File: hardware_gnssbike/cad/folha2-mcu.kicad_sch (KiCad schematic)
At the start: 7 parts, among them J201 Tag-Connect TC2030-NL, U201 MinewSemi ME54BS13

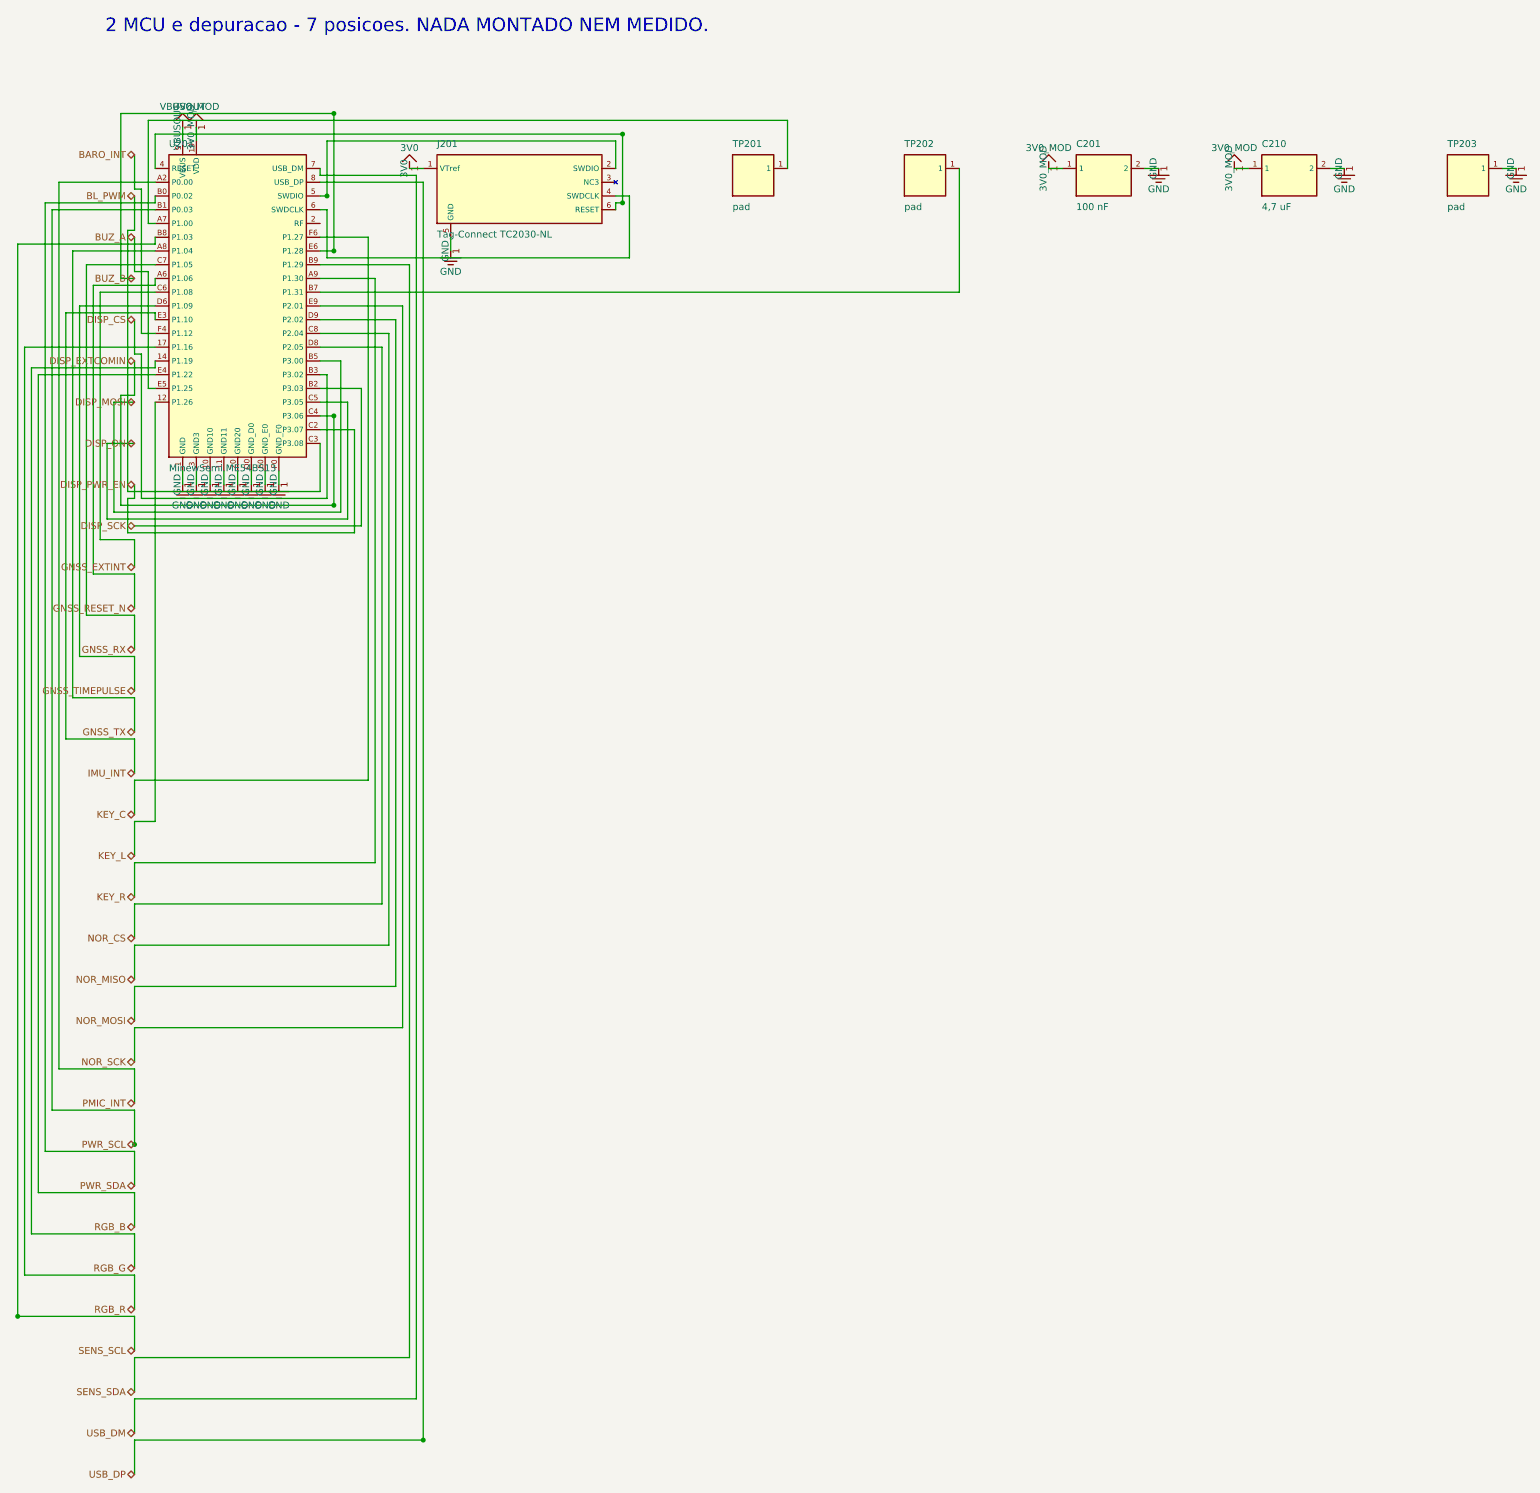
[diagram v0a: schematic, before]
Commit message: feat(hardware): the test points, a readable silkscreen, and paper that fits
Eleven of the sixteen test points of 06-conectores-e-pontos-de-teste.md were
not on the board. Only the three of the console sheet existed; a rail you
cannot put a probe on is a rail you cannot debug. VBUS, VBUSOUT, VBAT, VSYS,
3V0, 1V8, SD3V0, 3V3BL, VBCKP, VINT and the ground reference are there now,
each beside the thing it measures, and each takes what is LEFT: placed with
the rest of JUNTO they pushed three decoupling capacitors off their rings,
one of them to 4.0 mm from a pin that wants 2. The two that are still
missing are the document's own absences - TP111 measures ST_STO, which the
AEM10900 datasheet does not have, and TP401 measures 5V0, from a regulator
not fitted with the JDI panel. The list lives in parts.TESTE and nets.py
refuses a point that names a net that does not exist.

The silkscreen named nothing. Every reference sat 1.8 mm above its part at
0.7 mm with a 0.1 mm stroke - below the floor every fab publishes - and 37
pairs of designators printed on top of each other. The text is at the fab
minimum now, 0.8 mm with 0.15, and each label is PLACED: candidates around
its own courtyard, nearest first, never over another label and preferably
not over another part's outline. 127 references, 0 overlapping. The mounting
hole's REF** is hidden; it names nothing and was the last label sitting on
another.

Ground: a mesh, not just a hem. Edge stitching keeps the boundary of the
surface pours from becoming a radiating slot and does nothing for the
middle, where a patch of pour that reaches the inner plane through a via
20 mm away is not ground at 2.4 GHz. A 4.0 mm grid of ground vias now
covers the board - under the 6.1 mm that is a tenth of a wavelength in
FR-4 - laid last, on what is free, so a stitch never costs a connection.

The router's search learned about pad fields. The neck beside a pad existed
only in emitir(), and emitir only ever sees paths the search already found,
so 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
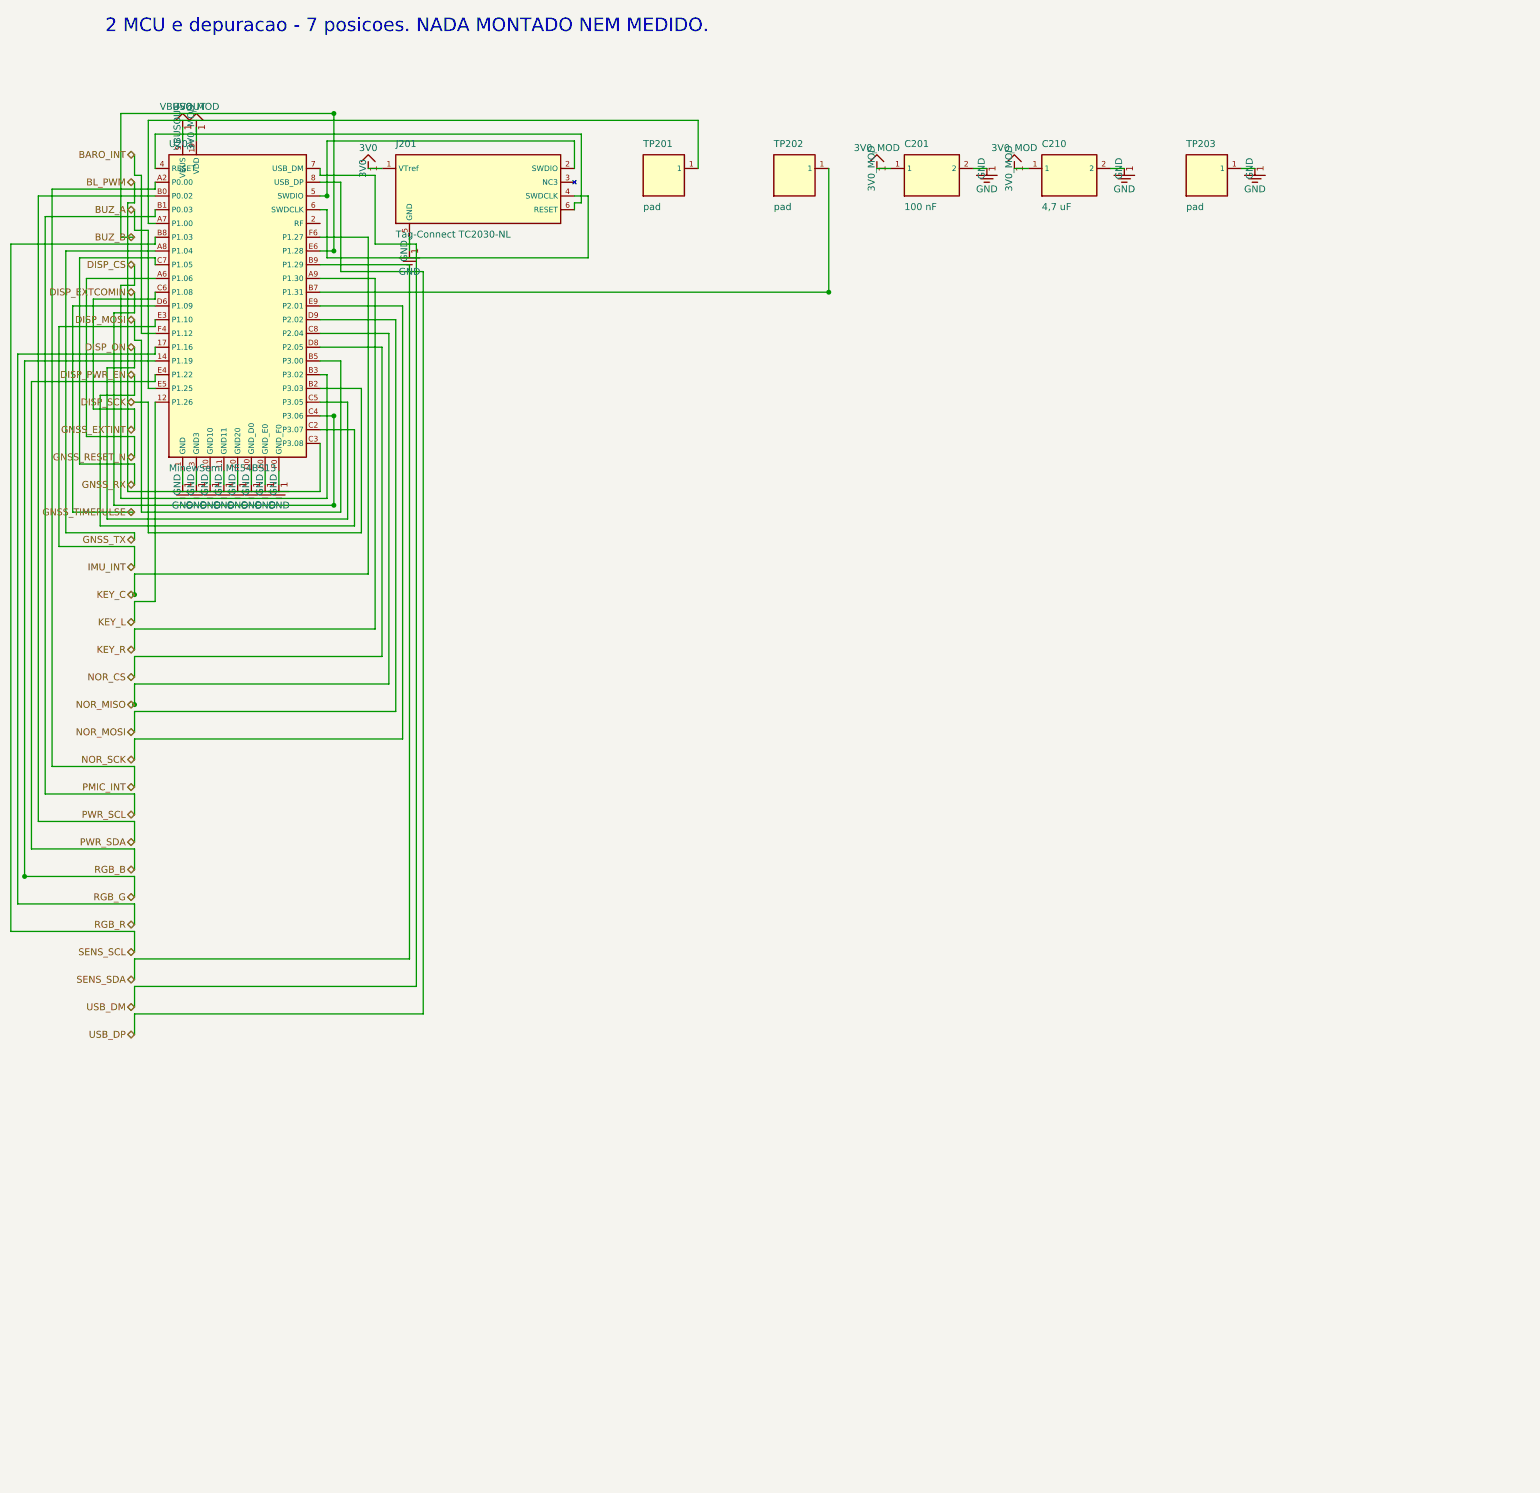
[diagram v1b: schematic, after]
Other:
- moved on the sheet: C201, C210, J201, TP201, TP202, TP203

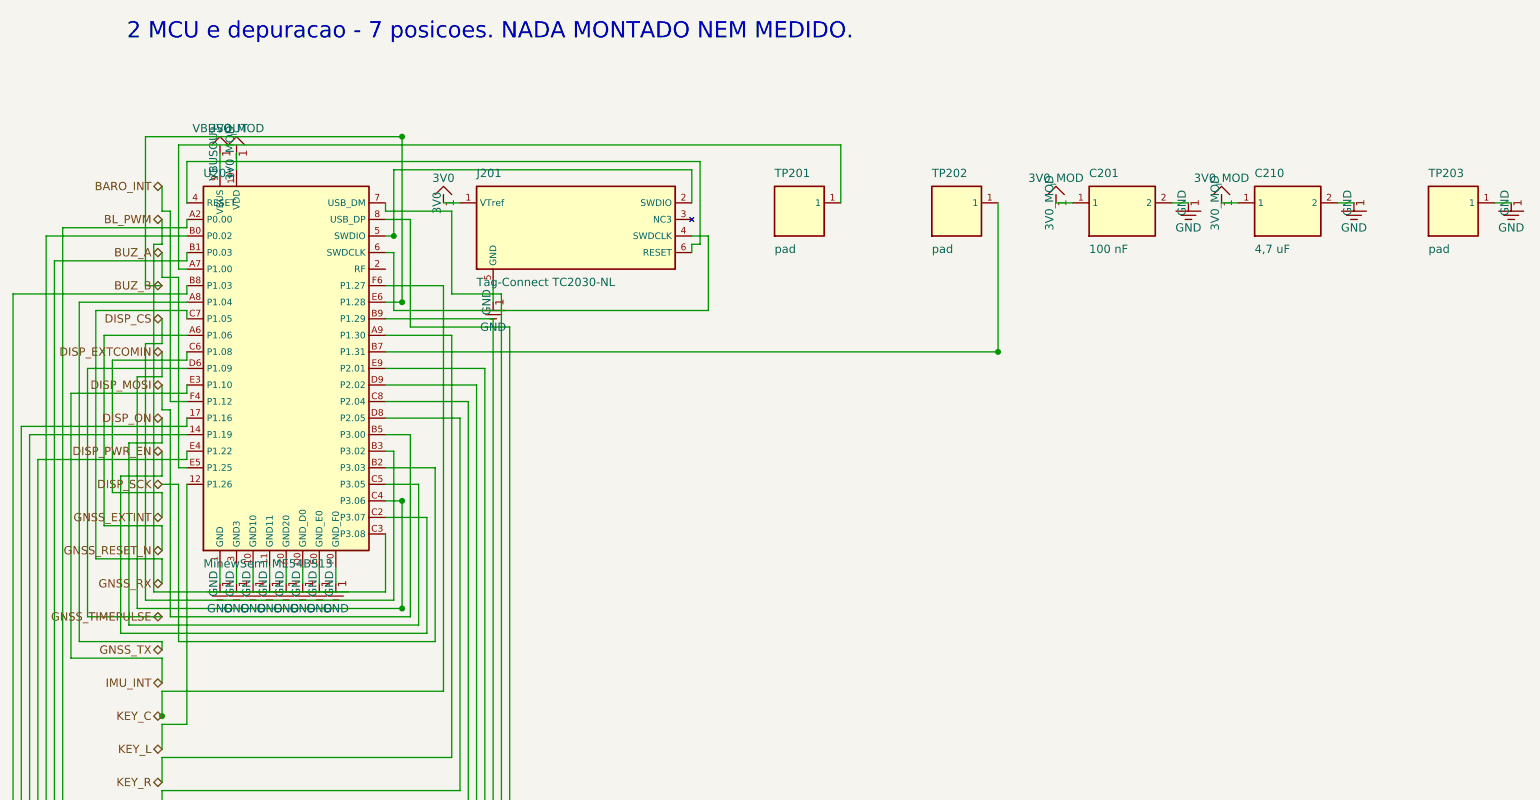
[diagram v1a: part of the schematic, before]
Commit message: feat(hardware): draw each part as its own symbol, not as a block
A rectangle with pin names down its sides is how an INTEGRATED CIRCUIT is
drawn, and only an integrated circuit. This generator drew all 127 parts
that way - resistors, ceramic capacitors, diodes, the TVS - and a sheet of
blocks joined by lines does not show a circuit.

Every class has its own symbol now, in the standard form, with the lead
axis on x and the body between -1.27 and +1.27 mm: a zigzag for a resistor
and a 0 ohm link (42 of them), two parallel plates for a ceramic capacitor
and a curved plate with a + for an electrolytic (31), four arcs for an
inductor (4), the same arcs inside a rectangle for a ferrite bead, which is
what tells the two apart, a zigzag with a diagonal arrow for the thermistor,
a triangle and a bar for a diode with arrows leaving it for an LED, two
contacts with a bar and a plunger for a key, a circle with a diagonal for
the buzzer, and a circle on the end of a lead for a test point. The 36 that
stay rectangles are the ones that should be: the ICs, the connectors and the
display. A two terminal part no longer prints pin numbers or pin names -
"1" and "2" on a resistor is noise, and the symbol already says which end is
which where it matters.

The power symbols had room reserved for the symbol and none for its NAME:
two ground pins two grid steps apart each got their own symbol, the symbols
did not collide, and the words printed over each other - "GNDGNDGND" along
the bottom of every chip. What is reserved now is the whole thing. With a
limit: the first cut let the stub run to fourteen grid steps looking for a
clear spot, and one of them crossed a component and split a net. A long stub
is worse than a crowded label, so it stops at eight and the label gives way.

One attempt is NOT in this commit, on purpose. Grouping every pin of a rail
on one edge into a single symbol - which is what a person draws - joins the
stubs with a line that runs along the part's edge and crosses w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
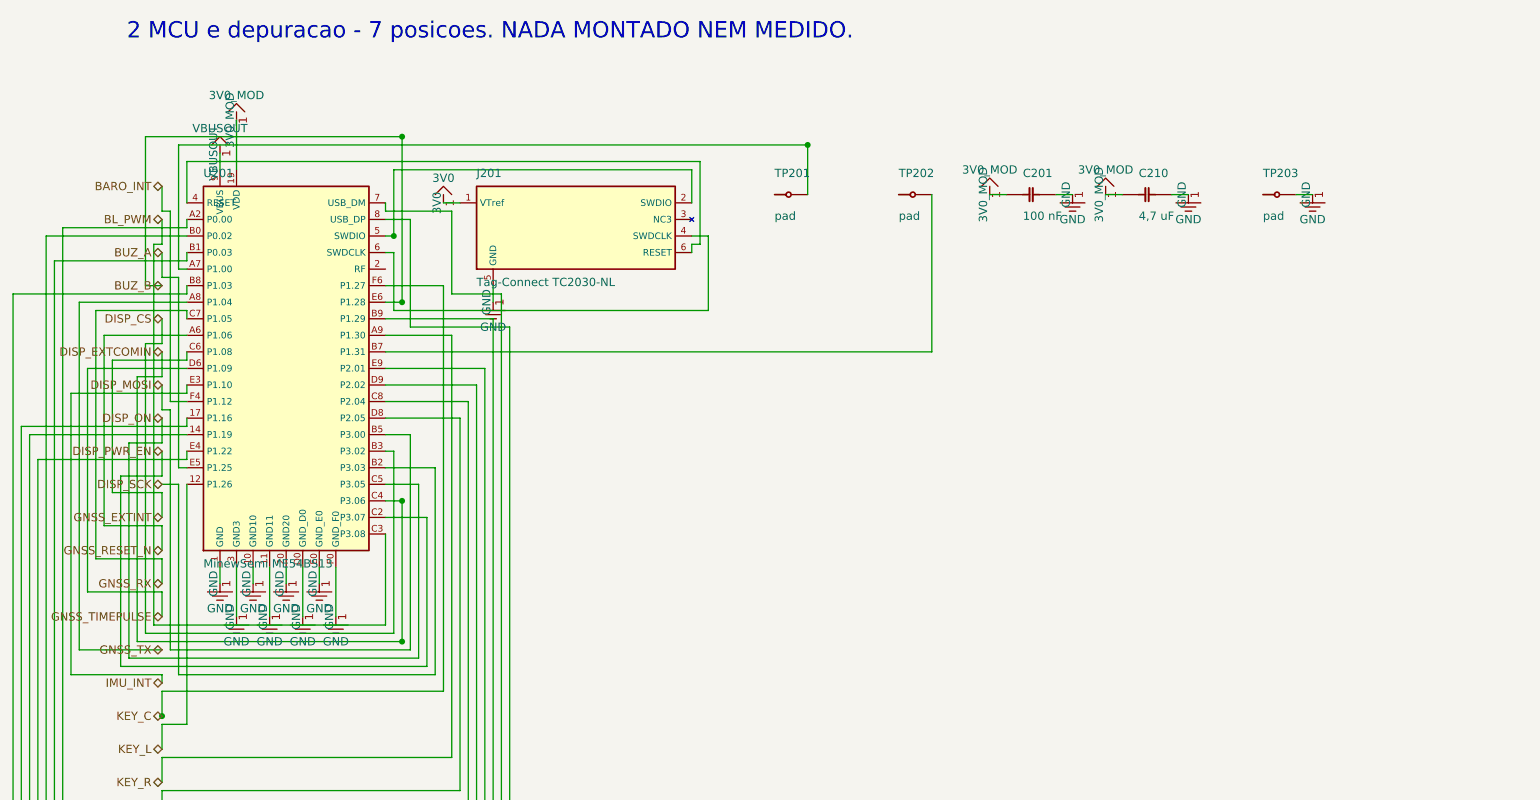
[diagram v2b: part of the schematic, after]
